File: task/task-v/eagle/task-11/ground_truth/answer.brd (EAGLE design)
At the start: 40 x 25 mm, 3 parts

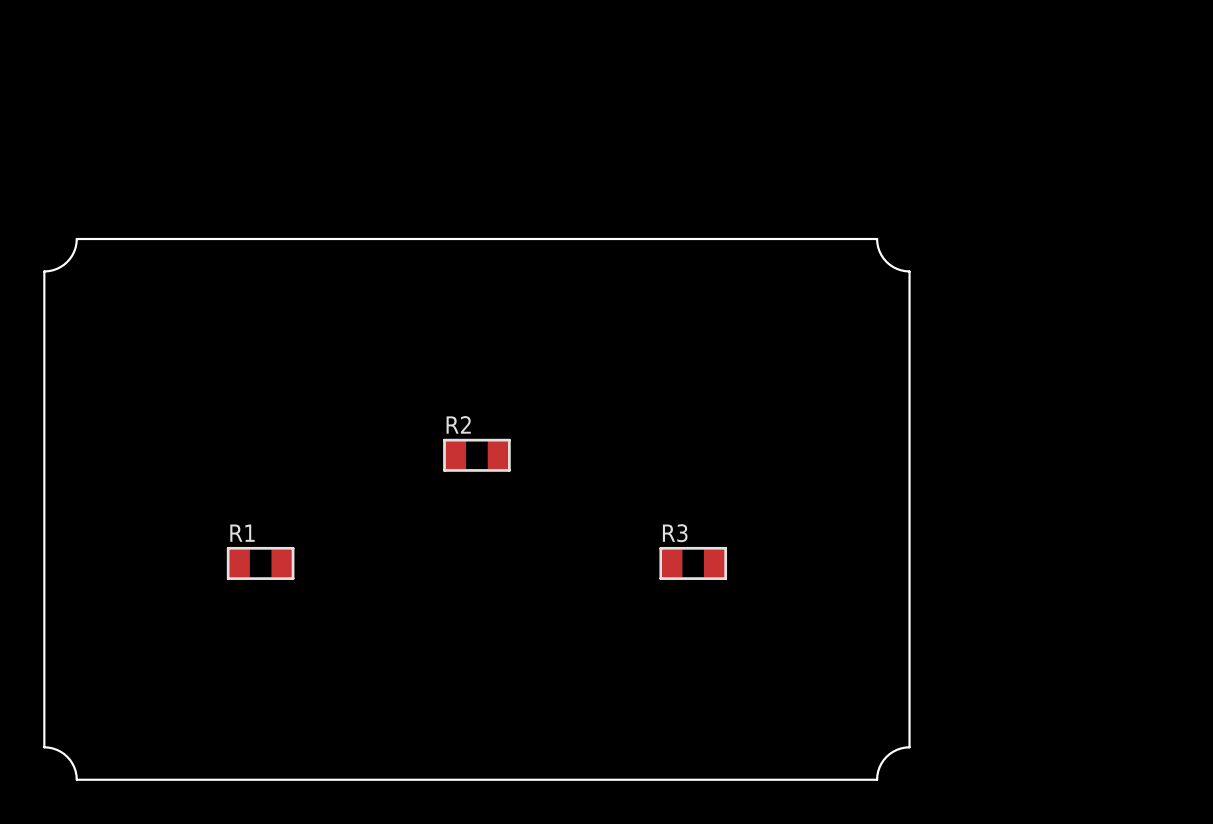
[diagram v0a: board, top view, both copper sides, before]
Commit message: Increase Eagle GUI task difficulty
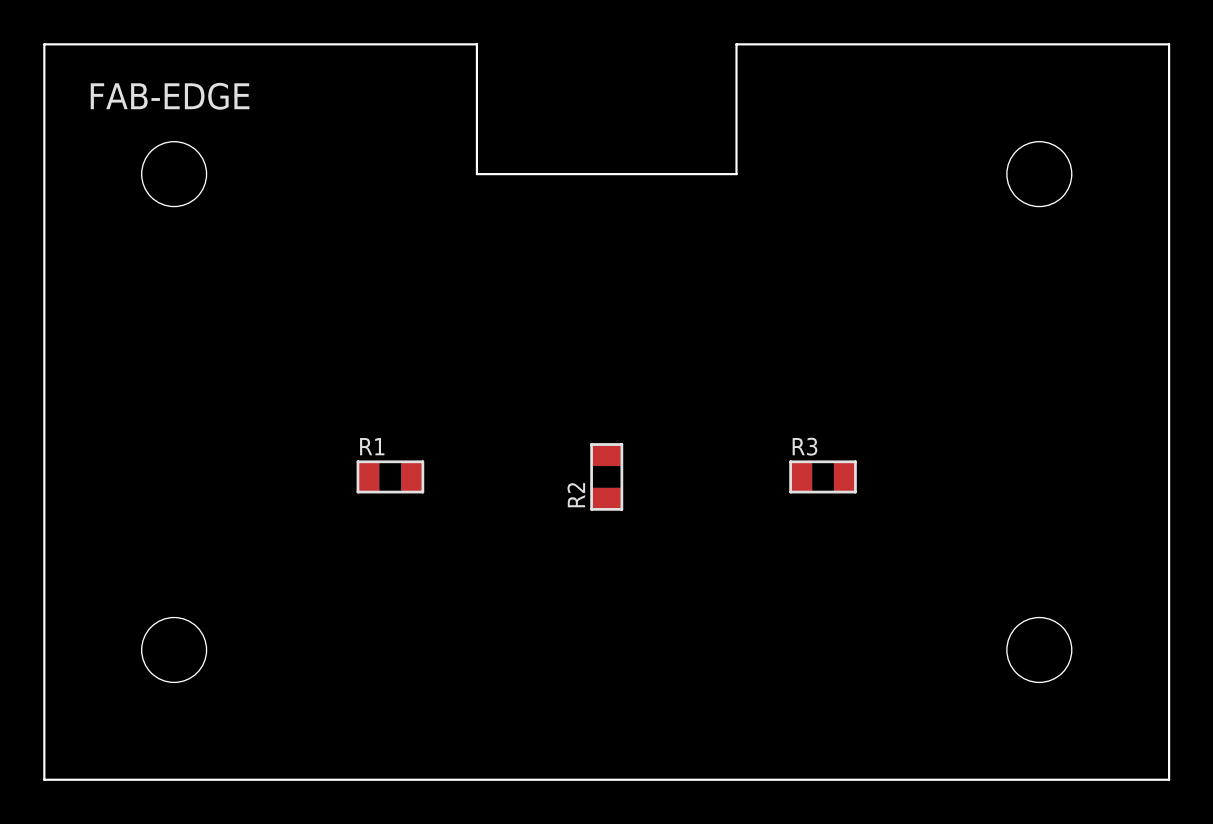
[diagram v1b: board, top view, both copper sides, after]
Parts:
- moved R1 7.21 mm to (16.0, 14.0)
- moved R3 7.21 mm to (36.0, 14.0)
- moved R2 6.08 mm to (26.0, 14.0), turned to 90 degrees
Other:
- board size 40 x 25 mm -> 52 x 34 mm
- board text added: "FAB-EDGE"
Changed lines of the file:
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@@
 <!DOCTYPE eagle SYSTEM "eagle.dtd">
 <eagle version="7.4.0">
-<drawing>
-<settings>
-<setting alwaysvectorfont="yes"/>
-<setting verticaltext="up"/>
-</settings>
-<grid distance="0.1" unitdist="mm" unit="mm" style="lines" multiple="1" display="no" altdistance="0.01" altunitdist="mm" altunit="mm"/>
-<layers>
-<layer number="1" name="Top" color="4" fill="1" visible="yes" active="yes"/>
-<layer number="16" name="Bottom" color="1" fill="1" visible="yes" active="yes"/>
-<layer number="17" name="Pads" color="2" fill="1" visible="yes" active="yes"/>
-<layer number="18" name="Vias" color="2" fill="1" visible="yes" active="yes"/>
-<layer number="20" name="Dimension" color="15" fill="1" visible="yes" active="yes"/>
-<layer number="21" name="tPlace" color="7" fill="1" visible="yes" active="yes"/>
-<layer number="22" name="bPlace" color="7" fill="1" visible="yes" active="yes"/>
-<layer number="25" name="tNames" color="7" fill="1" visible="yes" active="yes"/>
-<layer number="27" name="tValues" color="7" fill="1" visible="yes" active="yes"/>
-<layer number="29" name="tStop" color="7" fill="3" visible="no" active="yes"/>
-<layer number="51" name="tDocu" color="7" fill="1" visible="yes" active="yes"/>
-</layers>
-<board>
-<plain>
-<wire x1="1.5" y1="0" x2="38.5" y2="0" width="0.1" layer="20"/>
-<wire x1="38.5" y1="0" x2="40.0" y2="1.5" width="0.1" layer="20" curve="-90"/>
-<wire x1="40.0" y1="1.5" x2="40.0" y2="23.5" width="0.1" layer="20"/>
-<wire x1="40.0" y1="23.5" x2="38.5" y2="25.0" width="0.1" layer="20" curve="-90"/>
-<wire x1="38.5" y1="25.0" x2="1.5" y2="25.0" width="0.1" layer="20"/>
-<wire x1="1.5" y1="25.0" x2="0" y2="23.5" width="0.1" layer="20" curve="-90"/>
-<wire x1="0" y1="23.5" x2="0" y2="1.5" width="0.1" layer="20"/>
-<wire x1="0" y1="1.5" x2="1.5" y2="0" width="0.1" layer="20" curve="-90"/>
-</plain>
-<attributes>
+  <drawing>
+    <settings>
+      <setting alwaysvectorfont="yes" />
+      <setting verticaltext="up" />
+    </settings>
+    <grid distance="0.1" unitdist="mm" unit="mm" style="lines" multiple="1" display="no" altdistance="0.01" altunitdist="mm" altunit="mm" />
+    <layers>
+      <layer number="1" name="Top" color="4" fill="1" visible="yes" active="yes" />
+      <layer number="16" name="Bottom" color="1" fill="1" visible="yes" active="yes" />
+      <layer number="17" name="Pads" color="2" fill="1" visible="yes" active="yes" />
+      <layer number="18" name="Vias" color="2" fill="1" visible="yes" active="yes" />
+      <layer number="20" name="Dimension" color="15" fill="1" visible="yes" active="yes" />
+      <layer number="21" name="tPlace" color="7" fill="1" visible="yes" active="yes" />
+      <layer number="22" name="bPlace" color="7" fill="1" visible="yes" active="yes" />
+      <layer number="25" name="tNames" color="7" fill="1" visible="yes" active="yes" />
+      <layer number="27" name="tValues" color="7" fill="1" visible="yes" active="yes" />
+      <layer number="29" name="tStop" color="7" fill="3" visible="no" active="yes" />
+      <layer number="51" name="tDocu" color="7" fill="1" visible="yes" active="yes" />
+    </layers>
+    <board>
+      <plain>
+        <wire x1="0" y1="0" x2="52" y2="0" width="0.1" layer="20" />
+        <wire x1="52" y1="0" x2="52" y2="34" width="0.1" layer="20" />
+        <wire x1="52" y1="34" x2="32" y2="34" width="0.1" layer="20" />
+        <wire x1="32" y1="34" x2="32" y2="28" width="0.1" layer="20" />
+        <wire x1="32" y1="28" x2="20" y2="28" width="0.1" layer="20" />
+        <wire x1="20" y1="28" x2="20" y2="34" width="0.1" layer="20" />
+        <wire x1="20" y1="34" x2="0" y2="34" width="0.1" layer="20" />
+        <wire x1="0" y1="34" x2="0" y2="0" width="0.1" layer="20" />
+        <hole x="6" y="6" drill="3.0" />
+        <hole x="46" y="6" drill="3.0" />
+        <hole x="46" y="28" drill="3.0" />
+        <hole x="6" y="28" drill="3.0" />
+        <text x="2" y="31" size="1.2" layer="21">FAB-EDGE</text>
+      </plain>
+      <attributes>
 </attributes>
-<variantdefs>
+      <variantdefs>
 </variantdefs>
-<classes>
-<class number="0" name="default" width="0" drill="0">
+      <classes>
+        <class number="0" name="default" width="0" drill="0">
 </class>
-</classes>
-<designrules>
-<description language="en">Default design rules</description>
-</designrules>
-<autorouter>
+      </classes>
+      <designrules>
+        <description language="en">Default design rules</description>
+      </designrules>
+      <autorouter>
 </autorouter>
-<elements>
-<element name="R1" library="synth" package="R0805" value="10k" x="10" y="10"/>
-<element name="R2" library="synth" package="R0805" value="10k" x="20" y="15"/>
-<element name="R3" library="synth" package="R0805" value="10k" x="30" y="10"/>
-</elements>
-<signals>
+      <elements>
+        <element name="R1" library="synth" package="R0805" value="10k" x="16" y="14" />
+        <element name="R2" library="synth" package="R0805" value="10k" x="26" y="14" rot="R90" />
+        <element name="R3" library="synth" package="R0805" value="10k" x="36" y="14" />
+      </elements>
+      <signals>
 </signals>
-</board>
-</drawing>
+    </board>
+  </drawing>
 </eagle>
